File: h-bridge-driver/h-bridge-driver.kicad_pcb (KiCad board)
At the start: 4 copper layers, 25.4 x 40.6 mm, 20 parts, among them J1 CON_HDR_100MILS_M_TH_2X8, J2 CON_TERM_BLK_1X2_TB008A-508-0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, Q1 TRX_NMOS_PJD40N04_L2_00001, Q2 TRX_NMOS_PJD40N04_L2_00001, Q3 TRX_NMOS_PJD40N04_L2_00001, Q4 TRX_NMOS_PJD40N04_L2_00001, U1 DRV_A4957SESTR-T

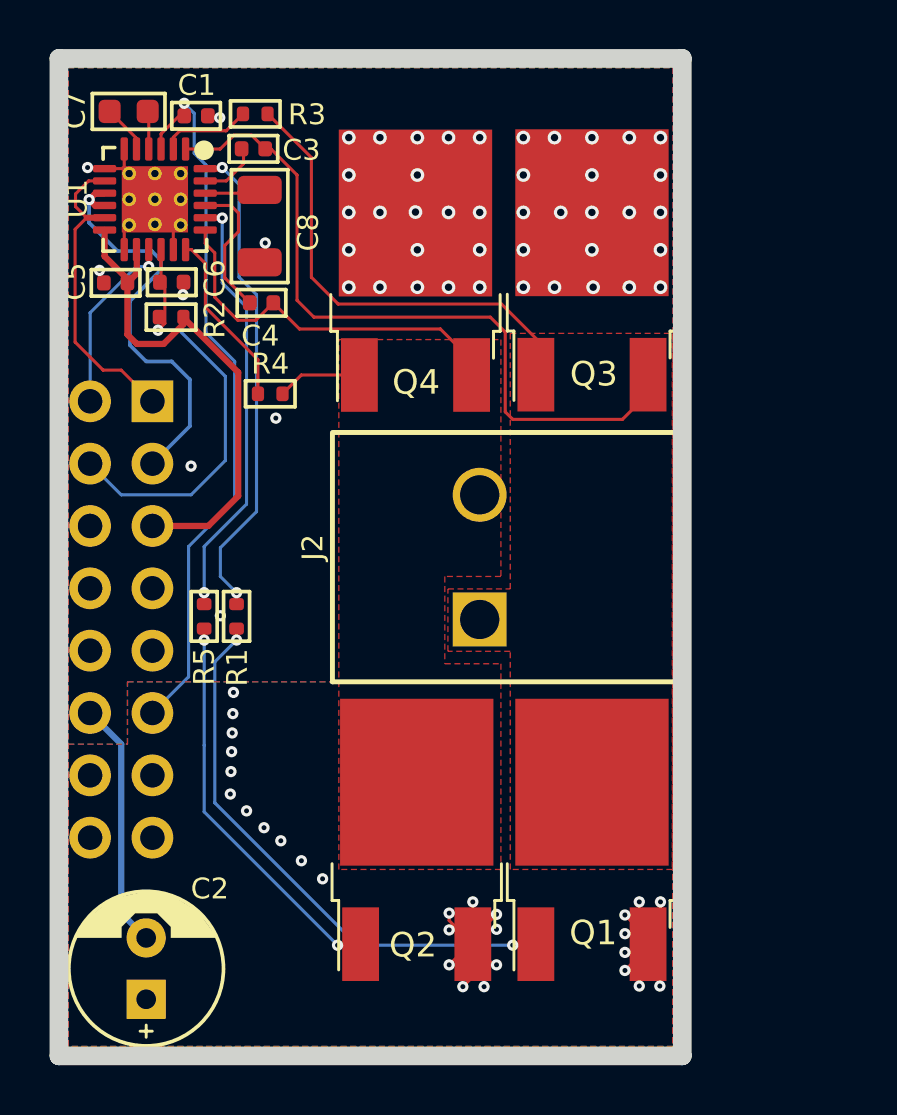
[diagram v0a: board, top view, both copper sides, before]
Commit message: Add motor driver page and I2C proteciton adapter, current & temp sensor
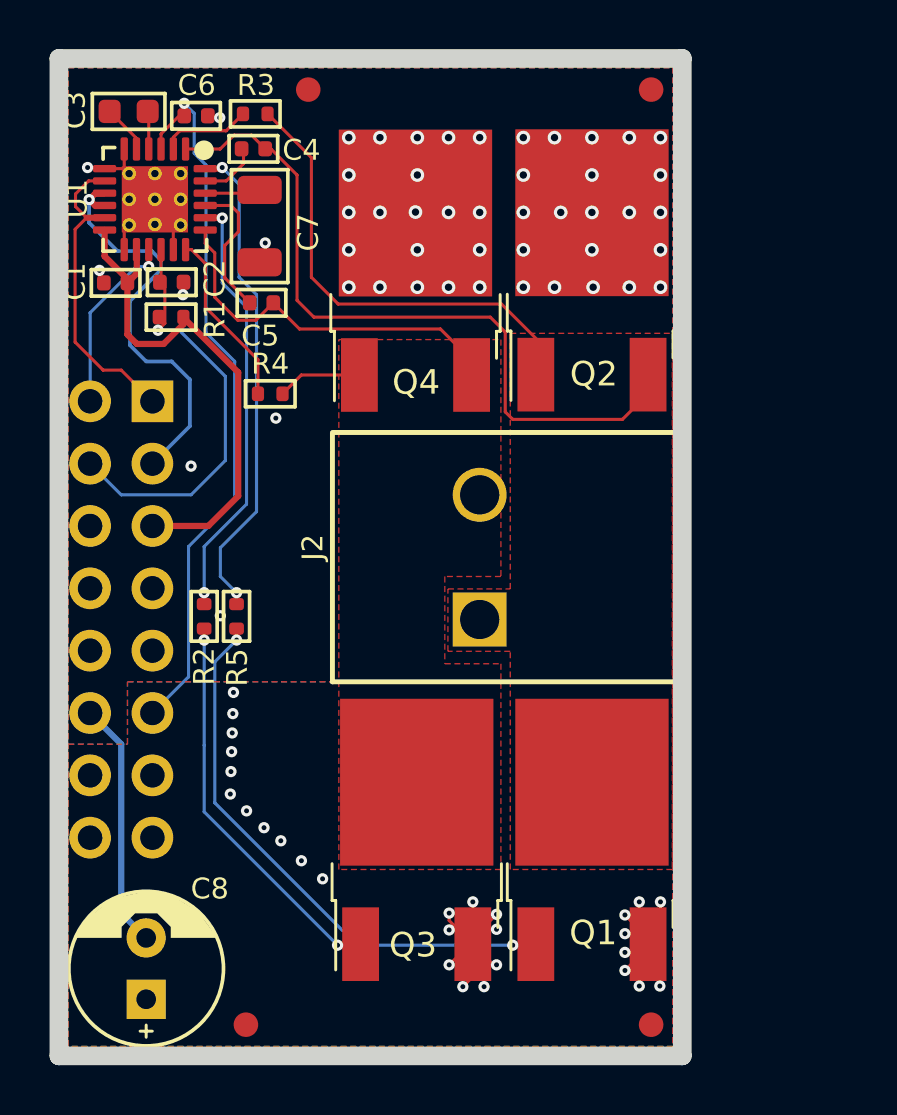
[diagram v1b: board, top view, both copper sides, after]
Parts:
- added F1: FID_1X1, connaxio-mechanical:FID_1X1, F.Cu at (138.0, 49.5)
- added F2: FID_1X1, connaxio-mechanical:FID_1X1, F.Cu at (124.1, 49.5)
- added F3: FID_1X1, connaxio-mechanical:FID_1X1, F.Cu at (121.5, 87.6)
- added F4: FID_1X1, connaxio-mechanical:FID_1X1, F.Cu at (138.0, 87.6)
- renumbered C5 to C1, C6 to C2, C7 to C3, C3 to C4, C4 to C5, C1 to C6, C8 to C7, C2 to C8, Q3 to Q2, Q2 to Q3, R2 to R1, R5 to R2, R1 to R5

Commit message: Move fuse to motor driver board Optimize board array schematic (hierarchical schematics)
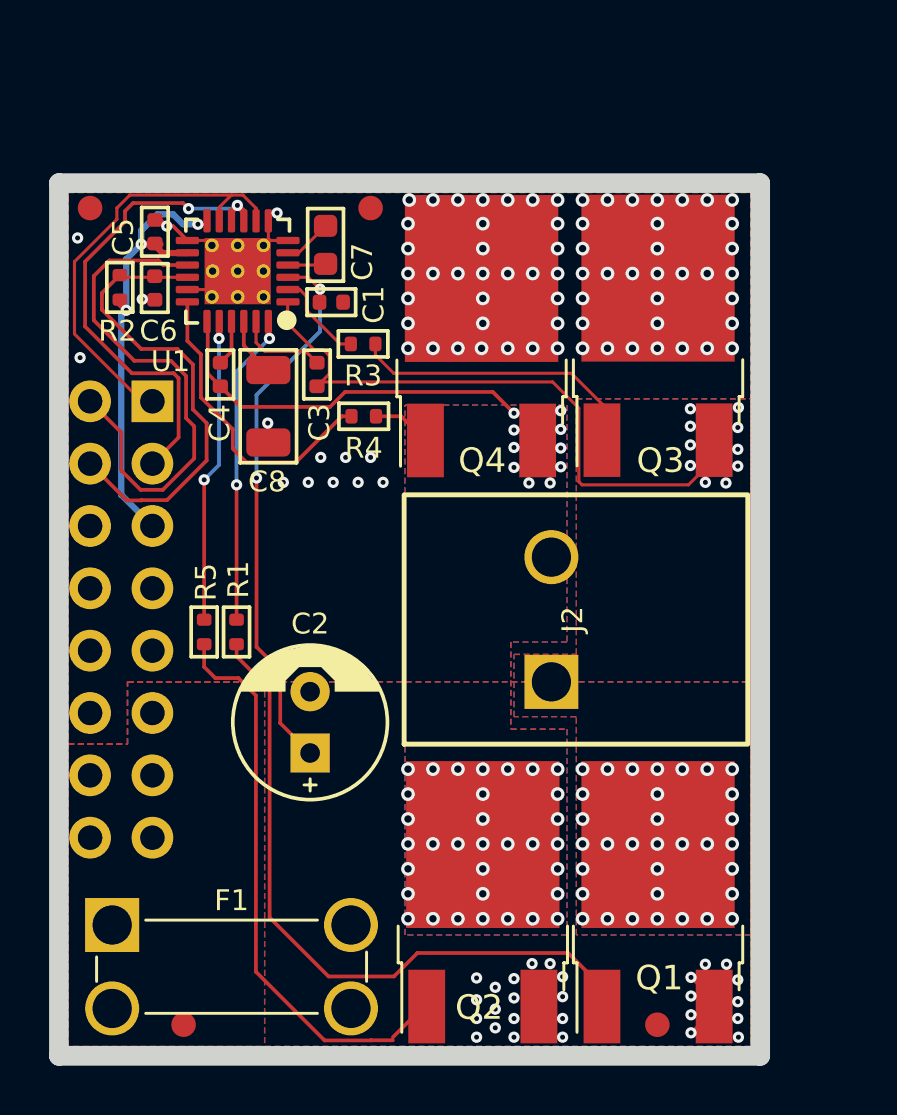
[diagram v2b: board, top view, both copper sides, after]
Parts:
- added F1: FUS_BLADE_MINI_3588-1, connaxio-connectors:FUS_BLADE_MINI_3588-1, F.Cu at (121.0, 85.3)
- moved F2 12.4 mm to (126.6, 54.4)
- moved C2 12.1 mm to (124.2, 75.3)
- moved R3 10.4 mm to (126.3, 59.9)
- moved F3 10.1 mm to (115.2, 54.4)
- moved C7 9.69 mm to (124.8, 55.9), turned to -90 degrees
- moved C3 9.55 mm to (124.4, 61.1), turned to -90 degrees
- moved C1 9.38 mm to (125.0, 58.2)
- moved C8 7.35 mm to (122.5, 62.4)
- moved U1 4.47 mm to (121.2, 56.9), turned to 180 degrees
- moved R4 3.92 mm to (126.3, 62.8)
- moved J2 3.87 mm to (134.0, 71.1)
- moved Q4 3.79 mm to (131.1, 59.6)
- moved Q3 3.79 mm to (138.3, 59.6)
- moved Q1 3.70 mm to (138.3, 82.6)
- moved Q2 3.70 mm to (131.2, 82.6)
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- renumbered C6 to C1, C8 to C2, C4 to C3, C5 to C4, C1 to C5, C2 to C6, C3 to C7, C7 to C8, F1 to F2, F2 to F3, F3 to F4, F4 to F5, Q3 to Q2, Q2 to Q3, R5 to R1, R1 to R2, R2 to R5
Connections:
- F4 pad 1: Vdrive -> /VIN
- J1 pad 11: Vdrive -> /VIN
- J1 pad 13: Vdrive -> /VIN
- J1 pad 14: Vdrive -> /VIN
- J1 pad 15: Vdrive -> /VIN
- J1 pad 16: Vdrive -> /VIN
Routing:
- net Vdrive: track 56.0 -> 29.3 mm
- net /FAULT: track 7.47 -> 21.3 mm, vias 1 -> 0
- net GND: track 21.0 -> 10.5 mm, vias 49 -> 80
- net Net-(Q2-Pad1): track 16.2 -> 23.5 mm, vias 2 -> 0
- net Net-(R1-Pad1): track 20.0 -> 12.7 mm
- net Net-(Q3-Pad1): track 19.1 -> 12.0 mm
- net Net-(R4-Pad1): track 7.24 -> 12.6 mm
- net /CTRLA: track 12.7 -> 18.0 mm
- net Net-(R5-Pad1): track 17.5 -> 12.4 mm
- net Net-(Q1-Pad1): track 23.0 -> 28.0 mm, vias 2 -> 0
- net /OUTA: track 30.0 -> 25.6 mm, vias 0 -> 43
- net Net-(C4-Pad1): track 5.79 -> 1.87 mm
- net /CTRLB: track 17.0 -> 20.3 mm, vias 1 -> 2
- net +3.3V: track 21.4 -> 19.0 mm, vias 0 -> 3
- net /RST: track 17.1 -> 19.3 mm, vias 1 -> 0
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- added copper zone on B.Cu, net /OUTA
- added copper zone on In1.Cu, net /OUTA
- added copper zone on In2.Cu, net /OUTA
- added copper zone on B.Cu, net /OUTB
- added copper zone on In1.Cu, net /OUTB
- added copper zone on In2.Cu, net /OUTB
- added copper zone on B.Cu, net /VIN
- added copper zone on F.Cu, net /VIN
- added copper zone on In1.Cu, net /VIN
- added copper zone on In2.Cu, net /VIN
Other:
- board size 25.4 x 40.6 mm -> 28.6 x 35.6 mm

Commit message: rename project, comple simple switch layout, fix thermal reliefs
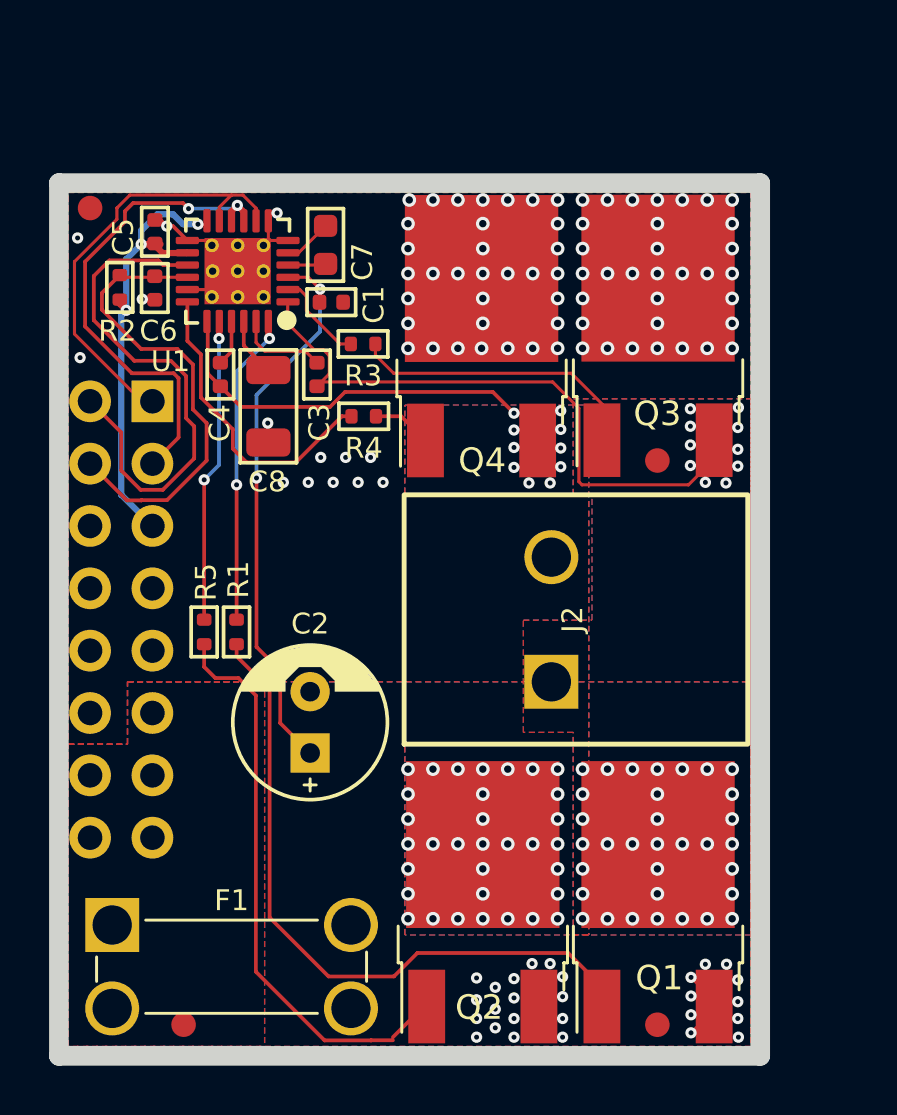
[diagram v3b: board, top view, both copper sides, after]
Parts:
- moved F2 15.6 mm to (138.3, 64.6)
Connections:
- F2 pad 1: GND -> /OUTA
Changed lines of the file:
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@@
     (property "Temperature" "-40°C to +105°C")
     (property "Voltage" "300V")
+    (zone_connect 1)
     (attr through_hole)
     (fp_text reference "J2" (at 0 0.8636 90 unlocked) (layer "F.SilkS")
@@
     (fp_rect (start -5.08 -6) (end 5.08 8) (layer "F.CrtYd") (width 0.05) (fill none))
     (pad "1" thru_hole rect (at -2.54 0 90) (size 2.2 2.2) (drill 1.6) (layers *.Cu *.Mask)
-      (net 5 "/OUTA") (pinfunction "1") (pintype "passive"))
+      (net 5 "/OUTA") (pinfunction "1") (pintype "passive") (zone_connect 1))
     (pad "2" thru_hole circle (at 2.54 0 90) (size 2.2 2.2) (drill 1.6) (layers *.Cu *.Mask)
       (net 6 "/OUTB") (pinfunction "2") (pintype "passive"))
@@
     (zone_connect 2)
     (attr smd)
-    (fp_text reference "Q3" (at 0.0986 5.08) (layer "F.SilkS")
+    (fp_text reference "Q3" (at -0.0284 3.1745) (layer "F.SilkS")
       (effects (font (size 1 1) (thickness 0.15)))
     )
@@
     (fp_line (start -0.375 2.27) (end -0.375 4.97) (layer "F.Fab") (width 0.1))
     (fp_line (start 1.905 2.27) (end 1.905 4.97) (layer "F.Fab") (width 0.1))
-    (pad "" smd rect (at 1.7 -0.6 90) (size 3.1 2.8) (layers "F.Paste"))
-    (pad "" smd rect (at -1.7 -0.6 90) (size 3.1 2.8) (layers "F.Paste"))
-    (pad "" smd rect (at -1.7 -4.1 90) (size 3.1 2.8) (layers "F.Paste"))
-    (pad "" smd rect (at 1.6875 -4.1 90) (size 3.1 2.8) (layers "F.Paste"))
+    (pad "" smd rect (at 1.7 -0.6 90) (size 3.1 2.8) (layers "F.Paste")
+      (zone_connect 2))
+    (pad "" smd rect (at -1.7 -0.6 90) (size 3.1 2.8) (layers "F.Paste")
+      (zone_connect 2))
+    (pad "" smd rect (at -1.7 -4.1 90) (size 3.1 2.8) (layers "F.Paste")
+      (zone_connect 2))
+    (pad "" smd rect (at 1.6875 -4.1 90) (size 3.1 2.8) (layers "F.Paste")
+      (zone_connect 2))
     (pad "1" smd rect (at -2.286 4.25) (size 1.5 3) (layers "F.Cu" "F.Paste" "F.Mask")
-      (net 14 "Net-(Q3-Pad1)") (pinfunction "G") (pintype "input"))
+      (net 14 "Net-(Q3-Pad1)") (pinfunction "G") (pintype "input") (zone_connect 2))
     (pad "2" smd rect (at 2.286 4.25) (size 1.5 3) (layers "F.Cu" "F.Paste" "F.Mask")
-      (net 5 "/OUTA") (pinfunction "D") (pintype "passive"))
+      (net 5 "/OUTA") (pinfunction "D") (pintype "passive") (zone_connect 2))
     (pad "3" smd rect (at 0 -2.35) (size 6.25 6.8) (layers "F.Cu" "F.Mask")
-      (net 2 "GND") (pinfunction "S") (pintype "passive"))
+      (net 2 "GND") (pinfunction "S") (pintype "passive") (zone_connect 2))
     (model ":CONNAXIO_KICAD_LIB_DIR:connaxio-sop.3dshapes/TO-252-3.wrl"
       (offset (xyz 0 0 0))
@@
   )
   (footprint "connaxio-mechanical:FID_1X1" (layer "F.Cu")
-    (at 126.619 54.356)
+    (at 138.303 64.643)
     (descr "Circular Fiducial, 1mm bare copper, 1 mm solder mask opening")
     (tags "fiducial")
@@
     (fp_circle (center 0 0) (end 1 0) (layer "F.Fab") (width 0.1) (fill none))
     (pad "1" smd circle (at 0 0) (size 1 1) (layers "F.Cu" "F.Mask")
-      (net 2 "GND") (pinfunction "1") (pintype "input") (zone_connect 2))
+      (net 5 "/OUTA") (pinfunction "1") (pintype "input") (zone_connect 2))
   )
   (footprint "connaxio-resistors:RES_0402_1005M" (layer "F.Cu")
@@
     (property "Temperature" "")
     (property "Voltage" "500V")
-    (zone_connect 2)
+    (zone_connect 1)
     (attr smd)
     (fp_text reference "F1" (at 0 -2.7 unlocked) (layer "F.SilkS")
@@
       (pts
         (xy 142.113 83.9729)
-        (xy 135.001 83.9729)
-        (xy 135.001 75.0829)
-        (xy 132.461 75.0829)
-        (xy 132.461 72.5429)
-        (xy 135.001 72.5429)
-        (xy 135.001 62.1289)
+        (xy 134.874 83.9729)
+        (xy 134.874 75.7179)
+        (xy 132.842 75.7179)
+        (xy 132.842 71.1459)
+        (xy 135.636 71.1459)
+        (xy 135.636 66.04)
+        (xy 134.874 66.04)
+        (xy 134.874 62.1289)
         (xy 142.113 62.1289)
       )
@@
     (polygon
       (pts
-        (xy 134.62 72.0349)
-        (xy 132.334 72.0349)
-        (xy 132.334 75.5909)
-        (xy 134.62 75.5909)
-        (xy 134.62 83.9729)
+        (xy 135.509 83.9729)
         (xy 128.016 83.9729)
         (xy 128.016 62.3829)
-        (xy 134.62 62.3829)
+        (xy 135.509 62.3829)
       )
     )

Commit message: Inverted motor controls for open-drain operation and manual switch override compatibility
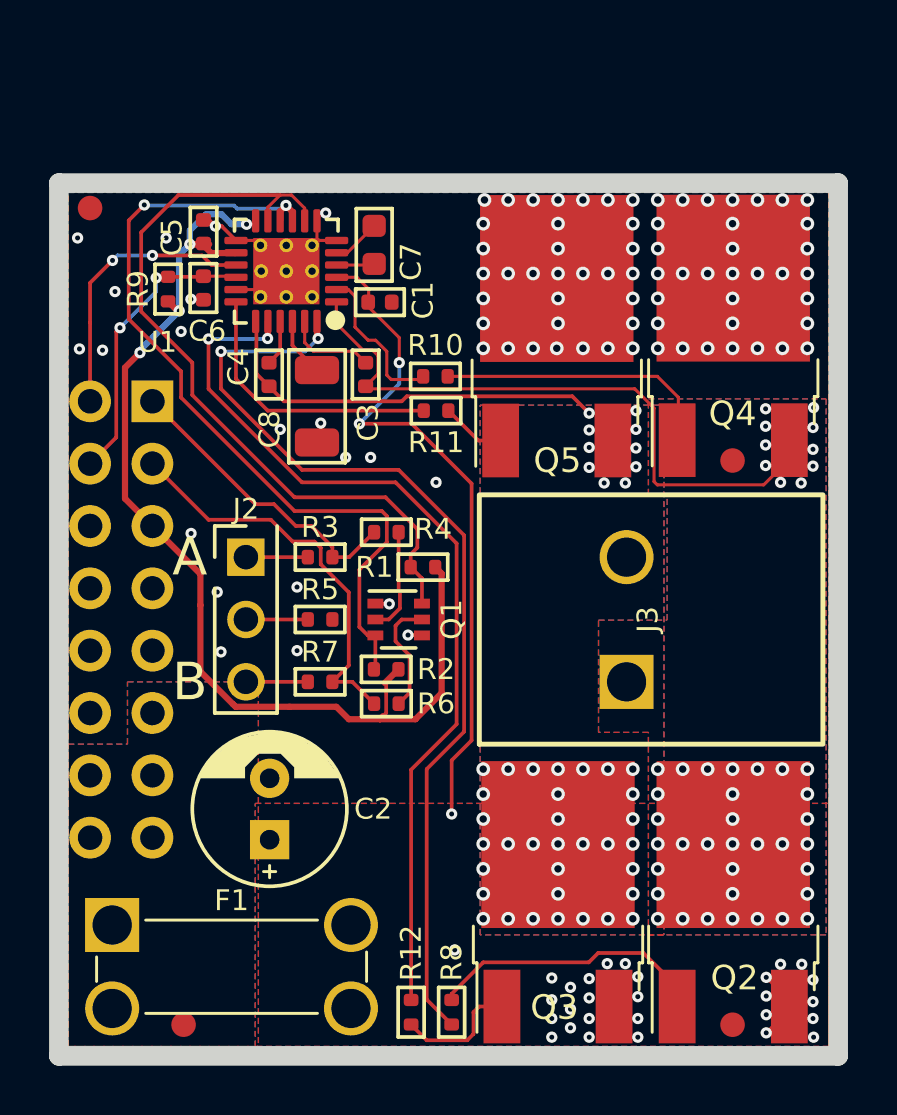
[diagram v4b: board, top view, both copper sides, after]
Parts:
- added J2: CON_HDR_100MILS_M_TH_1X3, connaxio-connectors:CON_HDR_100MILS_M_TH_1X3, F.Cu at (121.5, 71.1)
- added Q1: TRX_2NPN_BC846S,115, connaxio-sop:SOT-363_SC-70-6, F.Cu at (127.8, 71.1)
- added R1: RES_12.4KΩ_1%_0402, connaxio-resistors:RES_0402_1005M, F.Cu at (128.8, 69.0)
- added R3: RES_226Ω_1%_0402, connaxio-resistors:RES_0402_1005M, F.Cu at (124.6, 68.6)
- added R4: RES_12.4KΩ_1%_0402, connaxio-resistors:RES_0402_1005M, F.Cu at (127.3, 67.6)
- added R5: RES_226Ω_1%_0402, connaxio-resistors:RES_0402_1005M, F.Cu at (124.6, 71.1)
- added R6: RES_12.4KΩ_1%_0402, connaxio-resistors:RES_0402_1005M, F.Cu at (127.3, 74.5)
- added R7: RES_226Ω_1%_0402, connaxio-resistors:RES_0402_1005M, F.Cu at (124.6, 73.7)
- added R9: RES_12.4KΩ_1%_0402, connaxio-resistors:RES_0402_1005M, F.Cu at (118.4, 57.7)
- R2: value RES_5.10KΩ_1%_0402 -> RES_12.4KΩ_1%_0402
- moved R2 19.0 mm to (127.3, 73.2), turned to 180 degrees
- moved R8 17.8 mm to (129.9, 87.1), turned to 90 degrees
- moved R12 17.6 mm to (128.3, 87.1)
- moved C2 3.90 mm to (122.5, 78.8)
- moved R10 3.23 mm to (129.3, 61.2), turned to 0 degrees
- moved F2 3.06 mm to (141.4, 64.6)
- moved F5 3.06 mm to (141.4, 87.6)
- moved J3 3.06 mm to (137.0, 71.1)
- moved Q2 3.06 mm to (141.4, 82.6)
- moved Q3 3.06 mm to (134.3, 82.6)
- moved Q4 3.06 mm to (141.4, 59.6)
- moved Q5 3.06 mm to (134.2, 59.6)
- moved R11 2.96 mm to (129.3, 62.6)
- moved C1 1.98 mm to (127.0, 58.2)
- moved C3 1.98 mm to (126.4, 61.1)
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- renumbered J2 to J3, Q1 to Q2, Q2 to Q3, Q3 to Q4, Q4 to Q5, R3 to R10, R4 to R11, R5 to R12, R1 to R8
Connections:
- net /FAULT renamed /~{FAULT}
- C6 pad 1: /RST -> /~{RST}
- J1 pad 1: /CTRLA -> /~{CTRLA}
- J1 pad 3: /CTRLB -> /~{CTRLB}
- J1 pad 4: /RST -> /~{RST}
- Q4 pad 1: Net-(Q3-Pad1) (its old number) -> Net-(Q4-Pad1)
- R10 pad 1: Net-(Q3-Pad1) (its old number) -> Net-(R10-Pad1)
- R10 pad 2: Net-(R3-Pad2) -> Net-(Q4-Pad1)
- R2 pad 2: /RST -> /SIGB
- U1 pad 10: /CTRLB -> /SIGB
- U1 pad 11: /CTRLA -> /SIGA
- U1 pad 16: /RST -> /~{RST}
- U1 pad 2: Net-(R3-Pad2) -> Net-(R10-Pad1)
- U1 pad 8: /CTRLA -> /SIGA
- U1 pad 9: /CTRLB -> /SIGB
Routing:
- net /SIGB: track 0.00 -> 33.9 mm, vias 0 -> 2
- net /SIGA: track 0.00 -> 31.5 mm
- net Net-(R8-Pad1): track 12.7 -> 39.8 mm
- net +3.3V: track 19.0 -> 46.0 mm, vias 3 -> 4
- net Net-(R12-Pad1): track 12.4 -> 37.2 mm
- net /CTRLB: track 20.3 -> 0.00 mm, vias 2 -> 0
- net /RST: track 19.3 -> 0.00 mm
- net Net-(Q3-Pad1): track 23.5 -> 5.06 mm
- net /CTRLA: track 18.0 -> 0.00 mm
- net /~{CTRLB}: track 0.00 -> 16.6 mm
- net Net-(Q2-Pad1): track 28.0 -> 11.5 mm
- net /~{CTRLA}: track 0.00 -> 12.3 mm
- net Net-(Q3-Pad1) (its old number): track 12.0 -> 0.00 mm
- net /~{RST}: track 0.00 -> 11.9 mm, vias 0 -> 2
- net Net-(Q4-Pad1): track 0.00 -> 11.5 mm
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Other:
- board size 28.6 x 35.6 mm -> 31.8 x 35.6 mm
- board text added: "A"
- board text added: "B"

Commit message: Add LEDs, fix NMOS, Add logos and infos on PCBs.
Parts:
- added D1: DIO_LED_GREEN_150060GS75000, connaxio-diodes:LED_0603_1608M, F.Cu at (127.0, 80.1)
- added G***: LOGO, LOGO, B.Cu at (117.5, 57.0)
- added G***: LOGO, LOGO, B.Cu at (135.4, 55.2)
- added R5: RES_5.10KΩ_1%_0402, connaxio-resistors:RES_0402_1005M, F.Cu at (127.0, 77.3)
- renumbered R9 to R10, R10 to R11, R11 to R12, R12 to R13, R5 to R6, R6 to R7, R7 to R8, R8 to R9
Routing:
- net Net-(D1-Pad1): track 0.00 -> 1.54 mm
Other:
- board text added: "${title} Rev ${rev} ${year}-${month} Licensed under CERN-OHL-W v2"
- board text added: "JLCJLCJLCJLC"
- board text added: "https://github.com/ Connaxio/production- controller-makroshield"
